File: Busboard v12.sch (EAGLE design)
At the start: 121 parts, among them J1_+15 PIN2F061.100, J2_+15 PIN2F061.100, J3_GND PIN2F061.100, J4_GND PIN2F061.100, J5_-15 PIN2F061.100, J6_-15 PIN2F061.100

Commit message: v12
- Aligned mounting holes
- All LEDS same orientation
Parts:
- renumbered +15V_DC_IN to +15V, -15V_DC_IN to -15V, GND_IN to GND
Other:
- moved on the sheet: D10, D11, D12, D13, D14, D2, D3, D4, D7, D8, D9

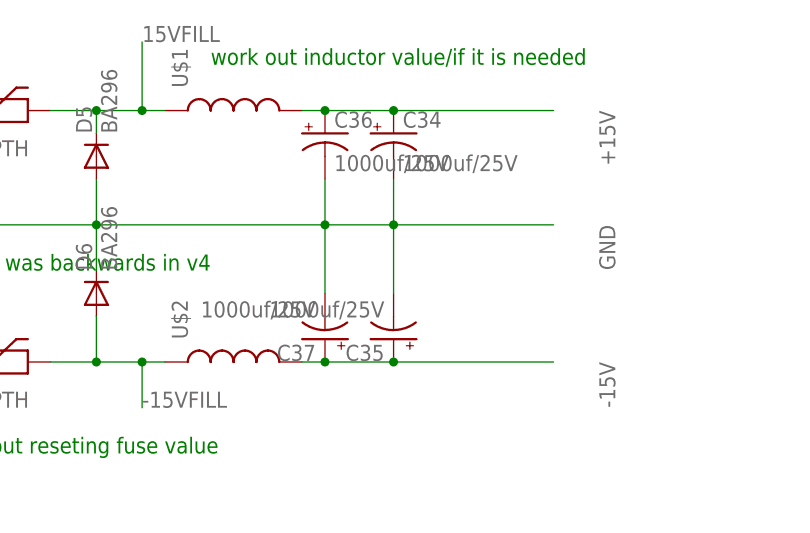
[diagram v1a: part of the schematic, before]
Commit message: updated .sch and .brd
i did another check over everything to make sure it lined up with the power sandwich, and added a 0.1uf 50v cap just after the inductor/ferrite bead to hopefully reduce ripple at the input.
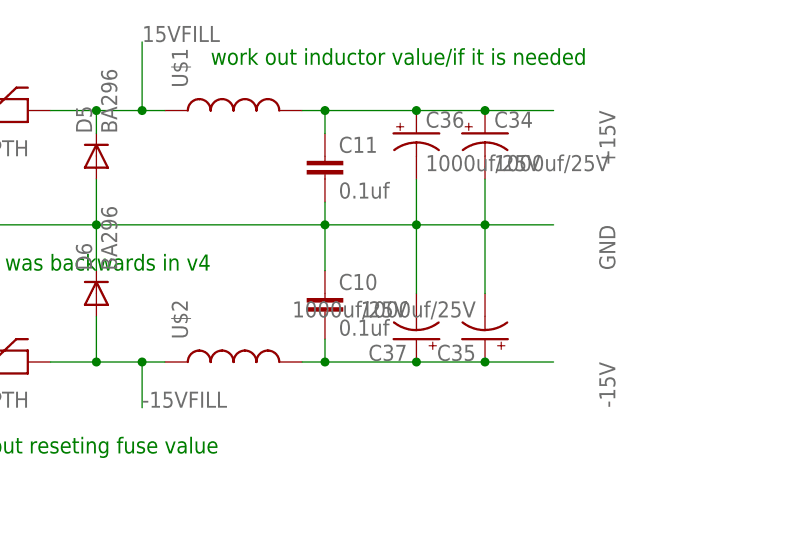
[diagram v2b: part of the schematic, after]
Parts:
- added C10, C11: 0.1uf, SparkFun-Capacitors:0.1UF-50V-20%(PTH)KIT-EZ
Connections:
- net +15V: now also C11.1
- net -15V: now also C10.2
- net GND: now also C10.1, C11.2
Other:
- moved on the sheet: C34, C35, C36, C37
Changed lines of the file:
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@@
 <part name="GND12" library="supply1" deviceset="GND" device=""/>
 <part name="GND13" library="supply1" deviceset="GND" device=""/>
+<part name="C10" library="SparkFun-Capacitors" deviceset="0.1UF-50V-20%(PTH)" device="KIT-EZ" value="0.1uf"/>
+<part name="C11" library="SparkFun-Capacitors" deviceset="0.1UF-50V-20%(PTH)" device="KIT-EZ" value="0.1uf"/>
 </parts>
 <sheets>
@@
 <instance part="R18" gate="G$1" x="561.34" y="71.12" rot="R90"/>
 <instance part="GND9" gate="1" x="523.24" y="27.94"/>
-<instance part="C34" gate="G$1" x="297.18" y="137.16"/>
-<instance part="C35" gate="G$1" x="297.18" y="114.3" rot="R180"/>
-<instance part="C36" gate="G$1" x="289.56" y="137.16"/>
-<instance part="C37" gate="G$1" x="289.56" y="114.3" rot="R180"/>
+<instance part="C34" gate="G$1" x="307.34" y="137.16"/>
+<instance part="C35" gate="G$1" x="307.34" y="114.3" rot="R180"/>
+<instance part="C36" gate="G$1" x="299.72" y="137.16"/>
+<instance part="C37" gate="G$1" x="299.72" y="114.3" rot="R180"/>
 <instance part="GND6" gate="1" x="121.92" y="88.9" rot="R180"/>
 <instance part="GND10" gate="1" x="226.06" y="88.9" rot="R180"/>
@@
 <instance part="GND12" gate="1" x="436.88" y="88.9" rot="R180"/>
 <instance part="GND13" gate="1" x="546.1" y="88.9" rot="R180"/>
+<instance part="C10" gate="G$1" x="289.56" y="116.84"/>
+<instance part="C11" gate="G$1" x="289.56" y="132.08"/>
 </instances>
 <busses>
@@
 <pinref part="U$1" gate="G$1" pin="2"/>
 <wire x1="287.02" y1="139.7" x2="289.56" y2="139.7" width="0.1524" layer="91"/>
-<wire x1="289.56" y1="139.7" x2="297.18" y2="139.7" width="0.1524" layer="91"/>
-<wire x1="297.18" y1="139.7" x2="314.96" y2="139.7" width="0.1524" layer="91"/>
+<wire x1="289.56" y1="139.7" x2="299.72" y2="139.7" width="0.1524" layer="91"/>
+<wire x1="299.72" y1="139.7" x2="307.34" y2="139.7" width="0.1524" layer="91"/>
+<wire x1="307.34" y1="139.7" x2="314.96" y2="139.7" width="0.1524" layer="91"/>
 <label x="320.04" y="139.7" size="1.778" layer="95" rot="R270"/>
 <pinref part="C34" gate="G$1" pin="+"/>
-<junction x="297.18" y="139.7"/>
+<junction x="307.34" y="139.7"/>
 <pinref part="C36" gate="G$1" pin="+"/>
+<junction x="299.72" y="139.7"/>
+<pinref part="C11" gate="G$1" pin="1"/>
+<wire x1="289.56" y1="137.16" x2="289.56" y2="139.7" width="0.1524" layer="91"/>
 <junction x="289.56" y="139.7"/>
 </segment>
@@
 <pinref part="U$2" gate="G$1" pin="2"/>
 <wire x1="287.02" y1="111.76" x2="289.56" y2="111.76" width="0.1524" layer="91"/>
-<wire x1="289.56" y1="111.76" x2="297.18" y2="111.76" width="0.1524" layer="91"/>
-<wire x1="297.18" y1="111.76" x2="314.96" y2="111.76" width="0.1524" layer="91"/>
+<wire x1="289.56" y1="111.76" x2="299.72" y2="111.76" width="0.1524" layer="91"/>
+<wire x1="299.72" y1="111.76" x2="307.34" y2="111.76" width="0.1524" layer="91"/>
+<wire x1="307.34" y1="111.76" x2="314.96" y2="111.76" width="0.1524" layer="91"/>
 <label x="320.04" y="111.76" size="1.778" layer="95" rot="R270"/>
 <pinref part="C35" gate="G$1" pin="+"/>
-<junction x="297.18" y="111.76"/>
+<junction x="307.34" y="111.76"/>
 <pinref part="C37" gate="G$1" pin="+"/>
+<junction x="299.72" y="111.76"/>
+<pinref part="C10" gate="G$1" pin="2"/>
+<wire x1="289.56" y1="114.3" x2="289.56" y2="111.76" width="0.1524" layer="91"/>
 <junction x="289.56" y="111.76"/>
 </segment>
@@
 </segment>
 <segment>
-<wire x1="297.18" y1="127" x2="289.56" y2="127" width="0.1524" layer="91"/>
+<wire x1="307.34" y1="127" x2="299.72" y2="127" width="0.1524" layer="91"/>
+<wire x1="299.72" y1="127" x2="289.56" y2="127" width="0.1524" layer="91"/>
 <wire x1="289.56" y1="127" x2="264.16" y2="127" width="0.1524" layer="91"/>
 <wire x1="264.16" y1="127" x2="241.3" y2="127" width="0.1524" layer="91"/>
-<wire x1="297.18" y1="127" x2="314.96" y2="127" width="0.1524" layer="91"/>
+<wire x1="307.34" y1="127" x2="314.96" y2="127" width="0.1524" layer="91"/>
 <junction x="264.16" y="127"/>
 <pinref part="D5" gate="1" pin="A"/>
@@
 <wire x1="264.16" y1="121.92" x2="264.16" y2="127" width="0.1524" layer="91"/>
 <pinref part="C35" gate="G$1" pin="-"/>
-<wire x1="297.18" y1="119.38" x2="297.18" y2="127" width="0.1524" layer="91"/>
-<junction x="297.18" y="127"/>
+<wire x1="307.34" y1="119.38" x2="307.34" y2="127" width="0.1524" layer="91"/>
+<junction x="307.34" y="127"/>
 <pinref part="C34" gate="G$1" pin="-"/>
-<wire x1="297.18" y1="127" x2="297.18" y2="132.08" width="0.1524" layer="91"/>
+<wire x1="307.34" y1="127" x2="307.34" y2="132.08" width="0.1524" layer="91"/>
 <pinref part="C37" gate="G$1" pin="-"/>
-<wire x1="289.56" y1="119.38" x2="289.56" y2="127" width="0.1524" layer="91"/>
+<wire x1="299.72" y1="119.38" x2="299.72" y2="127" width="0.1524" layer="91"/>
+<junction x="299.72" y="127"/>
+<pinref part="C36" gate="G$1" pin="-"/>
+<wire x1="299.72" y1="127" x2="299.72" y2="132.08" width="0.1524" layer="91"/>
+<label x="233.68" y="132.08" size="1.778" layer="95"/>
+<pinref part="C11" gate="G$1" pin="2"/>
+<wire x1="289.56" y1="129.54" x2="289.56" y2="127" width="0.1524" layer="91"/>
 <junction x="289.56" y="127"/>
-<pinref part="C36" gate="G$1" pin="-"/>
-<wire x1="289.56" y1="127" x2="289.56" y2="132.08" width="0.1524" layer="91"/>
-<label x="233.68" y="132.08" size="1.778" layer="95"/>
-</segment>
-<segment>
+<pinref part="C10" gate="G$1" pin="1"/>
+<wire x1="289.56" y1="127" x2="289.56" y2="121.92" width="0.1524" layer="91"/>
+</segment>
+<segment>

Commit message: Add files via upload
Fixing some dumb mistakes based on building the v12 prototype. had some backward caps and should have picked a lower trip thresh for the polyfuse.
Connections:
- net -15V: now also C35.-, C37.-; no longer C35.+, C37.+
- net GND: now also C17.+, C23.+, C28.+, C33.+, C35.+, C37.+, C5.+, C9.+; no longer 7.GND, 9.GND, C17.-, C23.-, C28.-, C33.-, C35.-, C37.-, C5.-, C9.-
- net N$1: now also C5.-; no longer C5.+
- net N$48: now also C23.-; no longer C23.+
- net N$57: now also C28.-; no longer C28.+
- net N$64: now also C33.-; no longer C33.+
- net N$7: now also C17.-; no longer C17.+
- net N$8: now also C9.-; no longer C9.+
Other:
- moved on the sheet: C17, C23, C28, C33, C35, C37, C5, C9
